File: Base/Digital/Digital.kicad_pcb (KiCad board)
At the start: 2 copper layers, 30 x 84 mm, 30 parts, among them J1 DC Jack, J2 IN, J3 OUT, J4 Conn_01x04_Pin, J5 Conn_01x05_Pin, U1 TPS73801, U2 TLE2426xD, U3 OPA1656

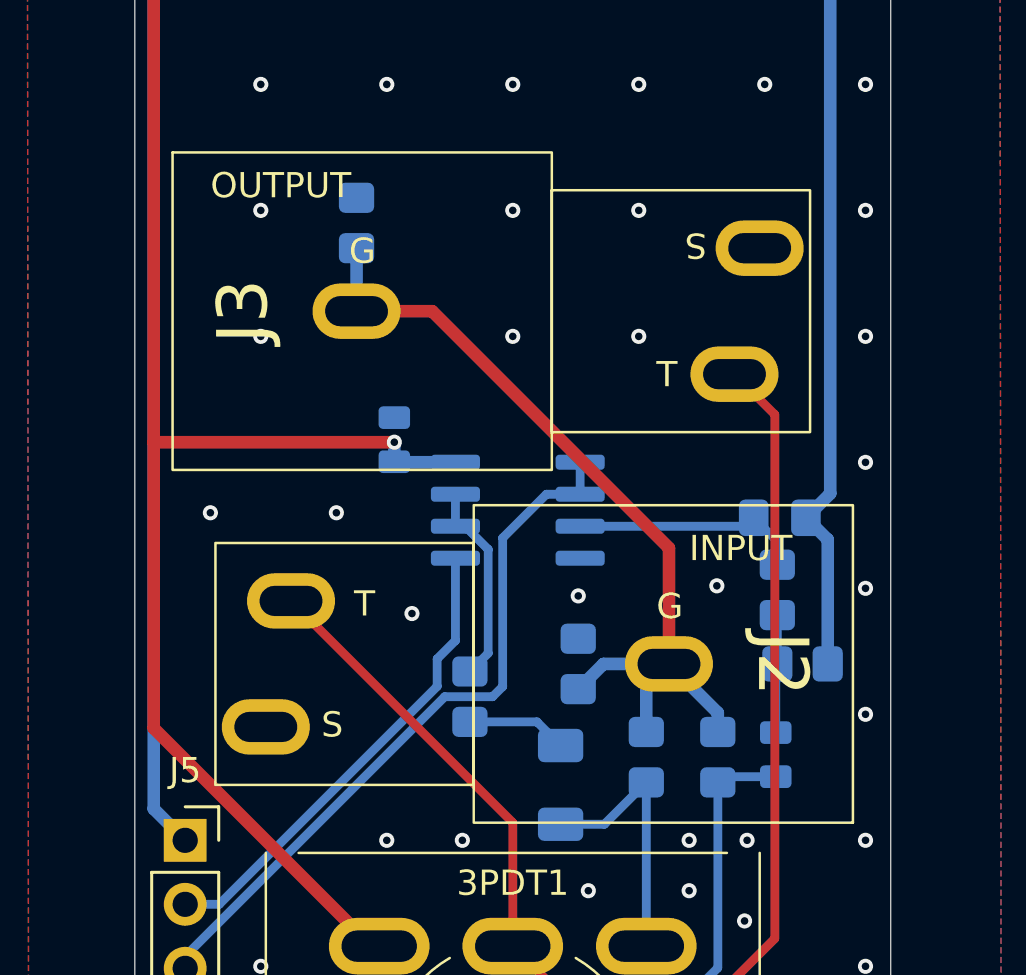
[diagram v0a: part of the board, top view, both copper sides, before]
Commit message: Move mono connectors out by 0.8mm each
Minimal trivial fixup to make the mono connectors poke out of the
enclosure just a tad more: this way we should have enough threads to
actually have the nut bite down on the jack.

Is the nut required? No.  But it should make things a bit stabler, and
let's do it right.

Is this enough? We'll see, but from a quick test-fit it looks just
barely sufficient, and I don't want to overdo it.

This is not worth doing new boards for, but I'm fixing it now so that
the next time I order more boards I will have this fixed.  I've meant to
do this for a long time, but just never got around to it.

Signed-off-by: Linus Torvalds <torvalds@linux-foundation.org>
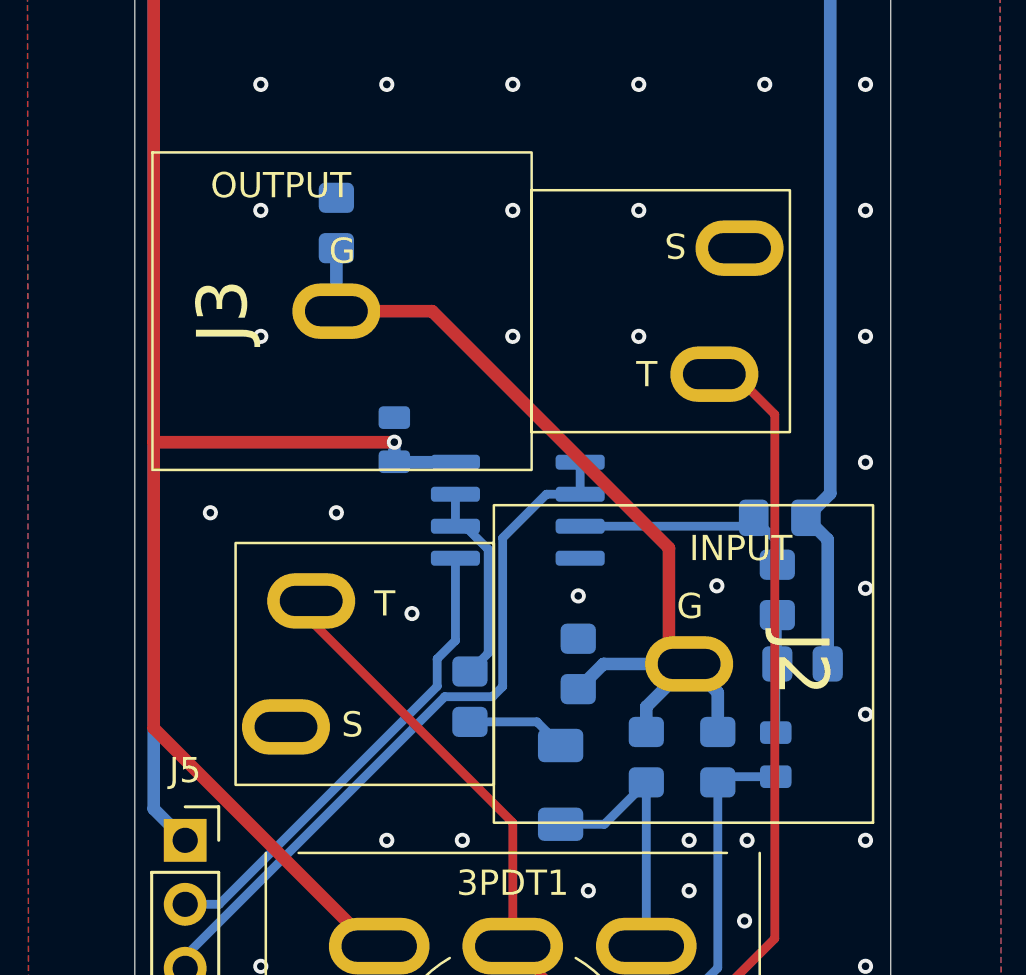
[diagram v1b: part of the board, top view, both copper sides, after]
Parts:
- moved J2 0.80 mm to (101.5, 118.0)
- moved J3 0.80 mm to (98.5, 104.0)
- moved R7 0.80 mm to (93.0, 100.5)
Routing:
- net GNDS: track 34.0 -> 34.8 mm
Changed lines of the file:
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@@
 	(footprint "Mylib:CK-6.35"
 		(layer "F.Cu")
-		(at 100.7 118 180)
+		(at 101.5 118 180)
 		(property "Reference" "J2"
 			(at -10 0 270)
@@
 	(footprint "Mylib:CK-6.35"
 		(layer "F.Cu")
-		(at 99.3 104)
+		(at 98.5 104)
 		(property "Reference" "J3"
 			(at -10 0 90)
@@
 	(footprint "Resistor_SMD:R_0805_2012Metric_Pad1.20x1.40mm_HandSolder"
 		(layer "B.Cu")
-		(at 93.8 100.5 -90)
+		(at 93 100.5 -90)
 		(descr "Resistor SMD 0805 (2012 Metric), square (rectangular) end terminal, IPC-7351 nominal with elongated pad for handsoldering. (Body size source: IPC-SM-782 page 72, https://www.pcb-3d.com/wordpress/wp-content/uploads/ipc-sm-782a_amendment_1_and_2.pdf), generated with kicad-footprint-generator")
 		(tags "resistor handsolder")
@@
 	)
 	(segment
-		(start 108.1375 119.9375)
-		(end 106.2 118)
+		(start 105.3 120.7)
+		(end 105.3 119.7)
 		(width 0.5)
 		(layer "B.Cu")
@@
 	)
 	(segment
-		(start 106.2 118)
-		(end 103.6 118)
+		(start 105.3 119.7)
+		(end 107 118)
 		(width 0.5)
 		(layer "B.Cu")
@@
 	)
 	(segment
-		(start 103.6 118)
-		(end 102.6 119)
+		(start 108.1375 119.1375)
+		(end 107 118)
 		(width 0.5)
 		(layer "B.Cu")
@@
 	)
 	(segment
-		(start 105.3 118.9)
-		(end 106.2 118)
+		(start 108.1375 120.7)
+		(end 108.1375 119.1375)
 		(width 0.5)
 		(layer "B.Cu")
@@
 	)
 	(segment
-		(start 108.1375 120.7)
-		(end 108.1375 119.9375)
+		(start 103.6 118)
+		(end 102.6 119)
 		(width 0.5)
 		(layer "B.Cu")
@@
 	)
 	(segment
-		(start 93.8 101.5)
-		(end 93.8 104)
+		(start 93 101.5)
+		(end 93 104)
 		(width 0.5)
 		(layer "B.Cu")
@@
 	)
 	(segment
-		(start 105.3 120.7)
-		(end 105.3 118.9)
+		(start 103.6 118)
+		(end 107 118)
 		(width 0.5)
 		(layer "B.Cu")

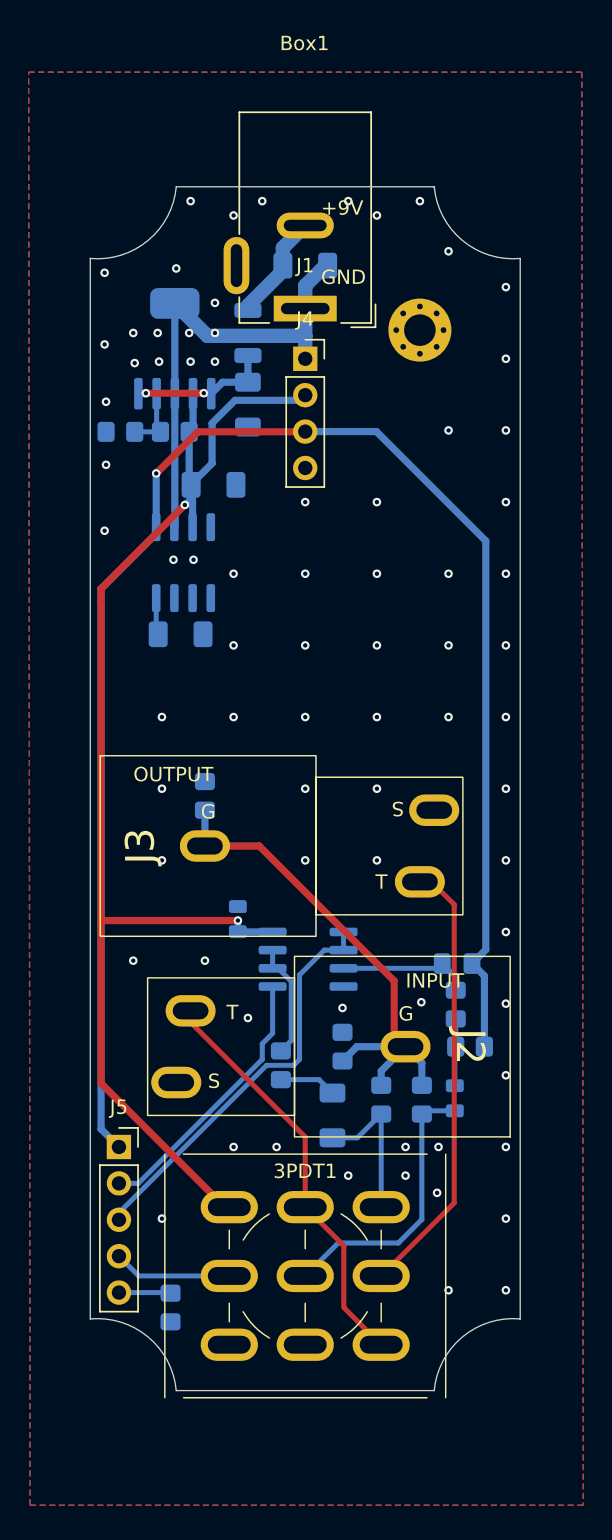
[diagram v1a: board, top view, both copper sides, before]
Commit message: Fix up some mis-designs in the the digital base board
First off, the LED power really should come from the +9V rail, not from
the LDO.  On the original VGND board, this didn't matter, since VIN was
the +9V rail with just the reverse voltage protection etc, but on this
board with the LDO, it's just wasting an LDO to make it drive the LED.

And worse than wasting the LDO on it, it makes the LED resistor overly
sensitive to the actual LED voltage, be it some red LED with a voltage
drop of 1.7V or a blue LED that drops 3.2V.

With the 9V rail, that's not such a huge deal, but with a 5V rail it's a
noticeable part of the whole available voltage and makes a big
difference for the current limiting resistor.

Ok, not really a fatal thing, and the fact that a super-efficient red
LED typically wants much less current than some fancy - but much less
efficient - purple LED would need means that you still do want to pick
the right resistor value, and the one on the schematic is just a
starting point.  But it was still not a good choice.

And I really need to sit down and learn more about the proper rules of
capacitive loads of op-amps and how to do this all right, but I'm pretty
sure I got the resistor very wrong on the output path to the capacitor.
This circuit does *not* want to slow down the charging and discharging
of the output capacitor, that just messes with the signal.

Now, I'm not sure I actually need the resistor to VREF - I think the
op-amp will drive the right voltage, but I need to think about it more.
In the meantime, add the resistor to VREF to make this look more like
the case I know works.

Signed-off-by: Linus Torvalds <torvalds@linux-foundation.org>
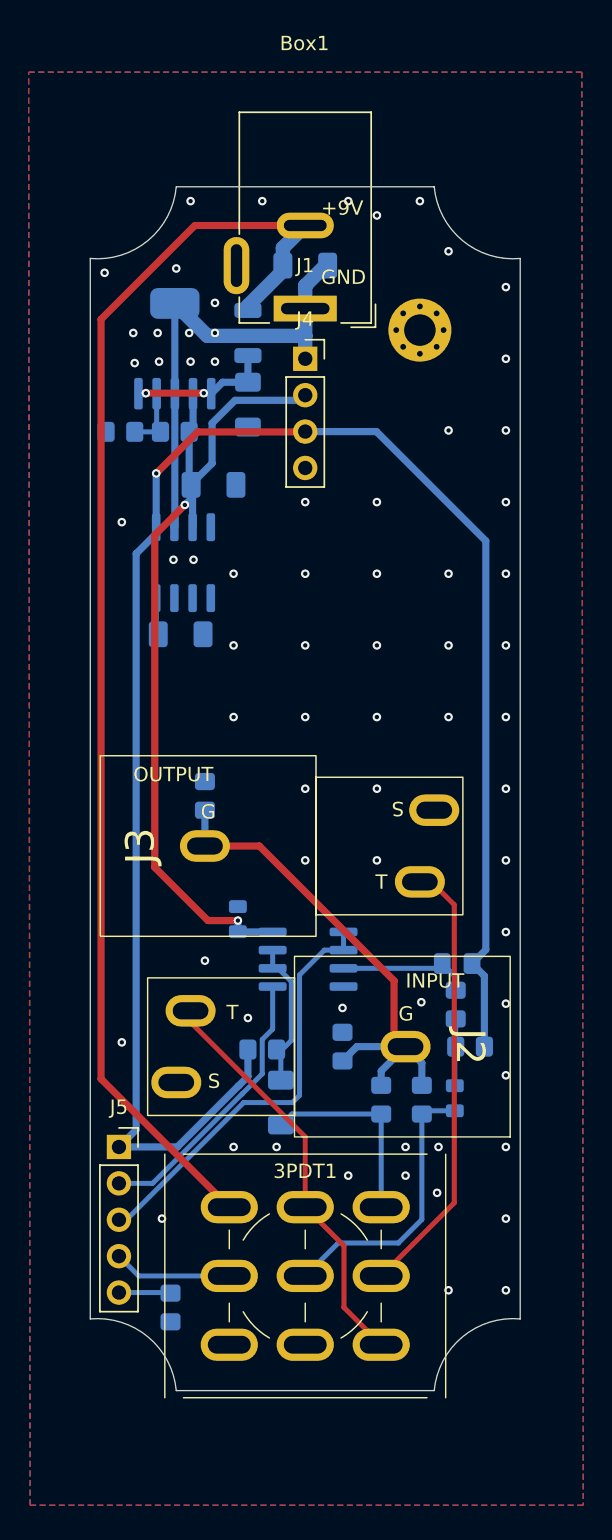
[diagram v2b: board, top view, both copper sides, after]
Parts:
- R3: value 10k -> 4.7k
- R9: value 1k -> 100k
- moved C8 3.71 mm to (98.3, 121.9)
- moved R9 1.70 mm to (97.0, 118.2), turned to 180 degrees
- renumbered C10 to C1, C3 to C2, C1 to C3
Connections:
- 3PDT1 pad 1: VIN -> +9V
- C8 pad 2: Net-(C8-Pad2) -> Net-(U3B--)
- R9 pad 2: Net-(C8-Pad2) -> GNDREF
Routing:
- net +9V: track 8.18 -> 89.8 mm
- net VIN: track 91.1 -> 58.3 mm
- net GNDREF: track 112.6 -> 123.9 mm
- net Net-(C8-Pad2): track 3.99 -> 0.00 mm
- net OUT^{RAW}: track 10.6 -> 13.8 mm
- net Net-(U3B--): track 8.10 -> 9.55 mm
- net OUT^{EFF}: track 19.0 -> 19.6 mm
- net GND: track 33.0 -> 32.8 mm, vias 75 -> 68

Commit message: Let's read the PT2399 datasheet, ok?
I'm sure I read the part where it said to use a 100uF capacitor, but I
clearly didn't internalize it.  And maybe it's overkill, but that thing
does claim to use up to 100mA, which is certainly more than any of my
other effects boards have ever approached.

Technically, I think we only really need one on the post-LDO +5V rail,
which is what the PT2399 obviously uses.  But I don't like having a big
output cap for the LDO without having something similar on the input
side too.

So my "let's not use electrolytics" model for the digital base board
needs to go.  But it's still true that this thing depends on the
TPS73801 for reverse voltage protection, and while maybe it would be
saner to just do a diode and a cheap regular LDO, that's not what this
is.

I'm just brute-forcing it, by getting a non-polar electrolytic 100uF
cap.  Is it bigger and more expensive than a regular one? Yes.  Do I
look like I care? No.  It's not like I'm cost-optimizing this for mass
production.  I'm doing single boards.

Is this going to matter? I don't know.  I don't even have any boards
with the PT2399 back yet.  But gosh-darn-it-to-heck, it's the right
thing to do.

Small nit: those caps will have to be put in lying down horizontally,
because they are too big and manly to fit under the effects board.  And
kicad doesn't have a footprint variant for that.  And I'm much too lazy
to make a custom footprint just for that.

So just leave enough space on the board, and try to remember when the
time comes to populate things (or when modifying the board design in the
future).

Signed-off-by: Linus Torvalds <torvalds@linux-foundation.org>
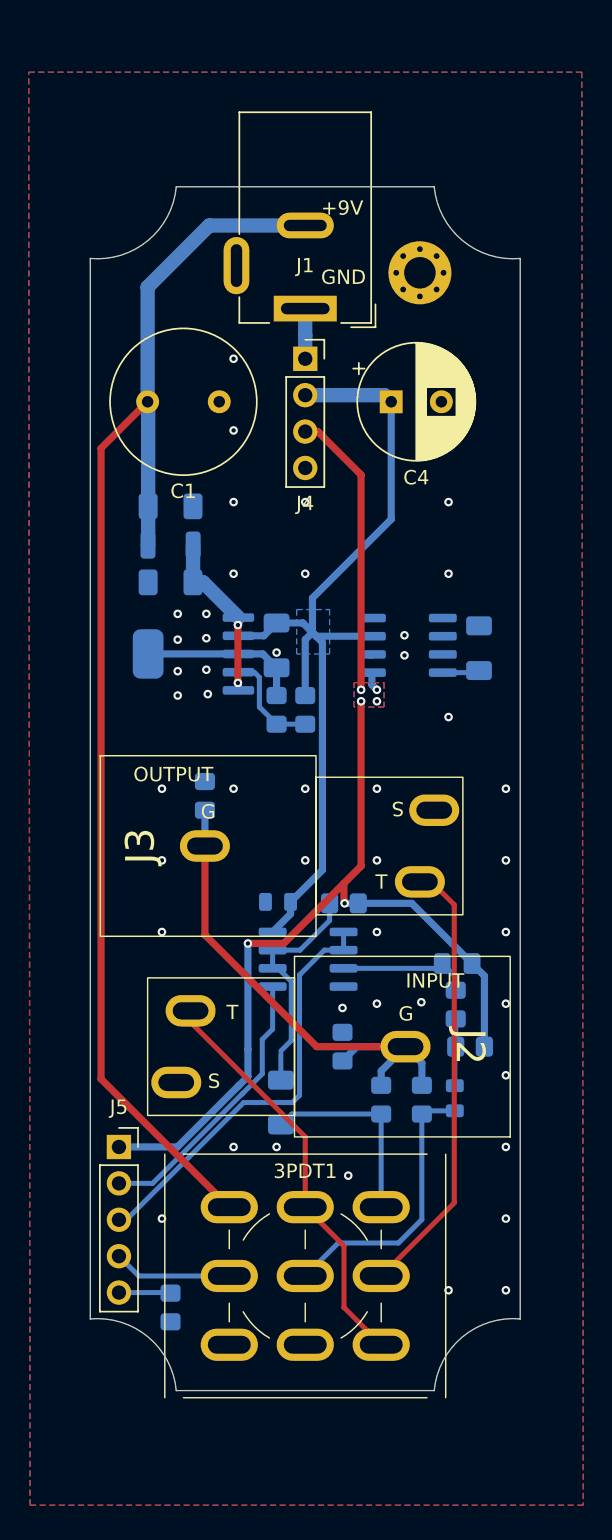
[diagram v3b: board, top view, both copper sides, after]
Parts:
- added C2: 10uF, Capacitor_SMD:C_1206_3216Metric_Pad1.33x1.80mm_HandSolder, B.Cu at (90.6, 80.3)
- added C4: 100uF, Capacitor_THT:CP_Radial_D8.0mm_P3.50mm, F.Cu at (106.0, 73.0)
- C1: value 47uF -> 100uF; footprint Capacitor_SMD:C_1206_3216Metric_Pad1.33x1.80mm_HandSolder -> Capacitor_THT:C_Radial_D10.0mm_H16.0mm_P5.00mm; moved to F.Cu
- moved R2 22.3 mm to (98.0, 94.5), turned to 90 degrees
- moved R1 21.4 mm to (100.0, 94.5), turned to -90 degrees
- moved U2 21.3 mm to (92.2, 90.6), turned to 180 degrees
- moved C6 20.8 mm to (112.1, 90.2), turned to 90 degrees
- moved U1 16.7 mm to (107.1, 90.0), turned to 0 degrees
- moved FB1 15.8 mm to (90.6, 83.0), turned to 0 degrees
- moved C3 13.5 mm to (90.6, 85.6), turned to 180 degrees
- moved C5 12.0 mm to (98.0, 90.0), turned to -90 degrees
- moved R9 11.7 mm to (102.7, 108.0), turned to 0 degrees
- moved C1 11.2 mm to (94.0, 73.0)
- moved H1 4.00 mm to (108.0, 64.0)
- moved C7 3.05 mm to (98.1, 107.9), turned to 180 degrees
- renumbered C8 to C10, C2 to C3, C3 to C5, C4 to C6, C5 to C7, C6 to C8, C7 to C9, U2 to U1, U1 to U2
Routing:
- net GNDREF: track 123.9 -> 81.7 mm, vias 1 -> 6
- net GND: track 32.8 -> 14.9 mm, vias 68 -> 45
- net Net-(U3B--): track 9.55 -> 15.6 mm
- net VIN: track 58.3 -> 61.9 mm, vias 2 -> 0
- net FB: track 4.19 -> 7.38 mm
- net +9V: track 89.8 -> 92.1 mm
- net Net-(U2-EN): track 9.81 -> 11.9 mm
- net GNDS: track 34.8 -> 36.5 mm
- added copper zone on B.Cu, net GNDREF
- added copper zone on F.Cu, net GNDREF
- added copper zone on B.Cu, net VIN

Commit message: More tweaking of the 5V (aka "digital") base board
I'm starting to think this is really what I should move over to, but
let's take all the good parts from the original VGND board.

My test board is much noisier than the latest VGND boards, and while
much of it is probably because I tried to initially avoid the
electrolytic caps, I do think the ferrite bead on the incoming power
ground may have actually mattered.

Because the noise looks somewhat similar to what the older boards looked
like on the oscilloscope, and things did get cleaner.  And the noise on
the new board shows up even in bypass mode, which implicates the ground
plane to me.

So let's bring over the ferrite on the power ground from the other
board, and try to make this board have cleaner power rails.

Signed-off-by: Linus Torvalds <torvalds@linux-foundation.org>
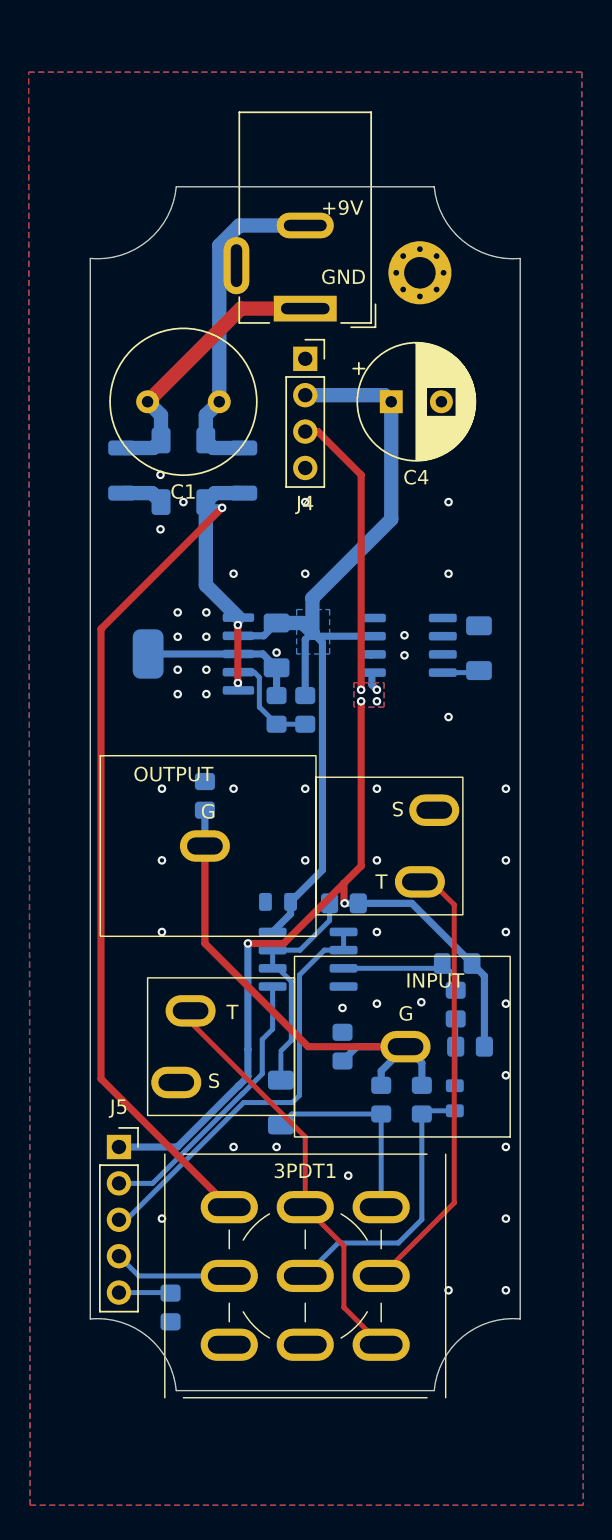
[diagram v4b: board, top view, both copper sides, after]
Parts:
- added FB2: FerriteBead, Inductor_SMD:L_1206_3216Metric, B.Cu at (87.2, 77.8)
- moved FB1 7.28 mm to (95.7, 77.8), turned to -90 degrees
- moved C3 5.67 mm to (91.5, 80.0)
- moved C2 4.69 mm to (91.5, 75.7), turned to 180 degrees
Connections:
- C1 pad 1: GND -> PWRIN
- C1 pad 2: +9V -> GNDIN
- C2 pad 1: +9V -> PWRIN
- C2 pad 2: GND -> GNDIN
- C3 pad 1: Net-(U2-EN) -> +9V
- FB1 pad 1: +9V -> PWRIN
- FB1 pad 2: Net-(U2-EN) -> +9V
- J1 pad 1: GND -> GNDIN
- J1 pad 2: +9V -> PWRIN
- J1 pad 3: unconnected-(J1-Pad3) -> PWRIN
- U2 pad 1: Net-(U2-EN) -> +9V
- U2 pad 5: Net-(U2-EN) -> +9V
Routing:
- net PWRIN: track 0.00 -> 23.2 mm
- net GNDIN: track 0.00 -> 19.6 mm
- net +9V: track 92.1 -> 74.1 mm, vias 0 -> 3
- net Net-(U2-EN): track 11.9 -> 0.00 mm, vias 2 -> 0
